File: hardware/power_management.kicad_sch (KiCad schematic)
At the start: 8 parts, among them J1 Conn_01x02, Q2 IRLML6402, U2 TP4056 breakout

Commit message: Made some items DNP and/or Exclude form Board
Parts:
- U2: now left out of the parts list
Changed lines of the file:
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@@
 		(unit 1)
 		(exclude_from_sim no)
-		(in_bom yes)
+		(in_bom no)
 		(on_board yes)
 		(dnp no)

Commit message: Added lables to all test points
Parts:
- TP16: value TestPoint -> BAT+
- TP17: value TestPoint -> BAT-
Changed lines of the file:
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@@
 			)
 		)
-		(property "Value" "TestPoint"
+		(property "Value" "BAT+"
 			(at 119.126 108.204 0)
 			(effects
@@
 			)
 		)
-		(property "Value" "TestPoint"
+		(property "Value" "BAT-"
 			(at 119.126 113.284 0)
 			(effects

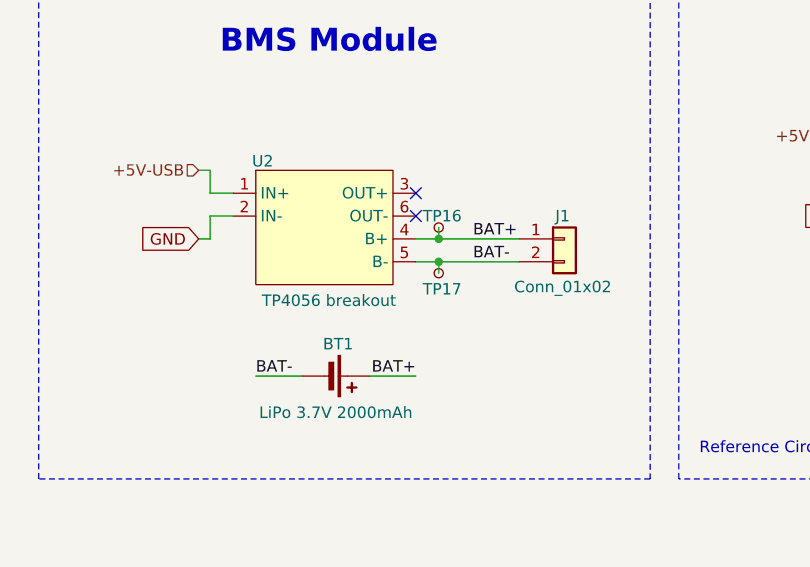
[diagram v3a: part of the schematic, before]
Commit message: Reviewed the Fields Table and marked all components that should not be populated. Then I runned rules check in the schematic and PCB
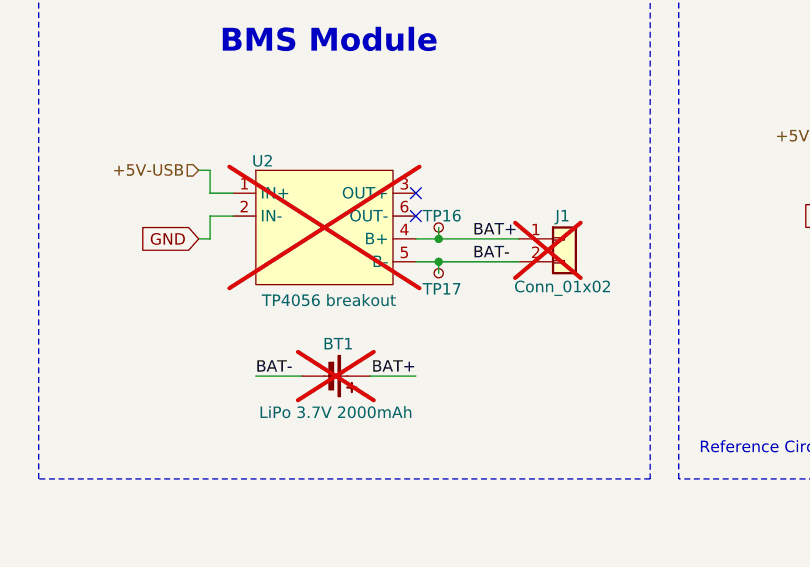
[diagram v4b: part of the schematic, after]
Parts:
- BT1, J1, U2: now not fitted
- TP16, TP17: now left out of the parts list
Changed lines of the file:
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@@
 		(unit 1)
 		(exclude_from_sim no)
-		(in_bom yes)
+		(in_bom no)
 		(on_board yes)
 		(dnp no)
@@
 		(in_bom no)
 		(on_board yes)
-		(dnp no)
+		(dnp yes)
 		(property "Reference" "J1"
 			(at 132.334 110.49 0)
@@
 		(in_bom no)
 		(on_board no)
-		(dnp no)
+		(dnp yes)
 		(property "Reference" "BT1"
 			(at 108.204 124.714 90)
@@
 		(unit 1)
 		(exclude_from_sim no)
-		(in_bom yes)
+		(in_bom no)
 		(on_board yes)
 		(dnp no)
@@
 		(in_bom no)
 		(on_board yes)
-		(dnp no)
+		(dnp yes)
 		(property "Reference" "U2"
 			(at 99.822 104.394 0)
